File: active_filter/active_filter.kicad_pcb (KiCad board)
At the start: 2 copper layers, 26.4 x 22.9 mm, 15 parts, among them J0 Conn_01x03_MountingPin, J1 Conn_01x03_MountingPin, U1 ADA4062-2

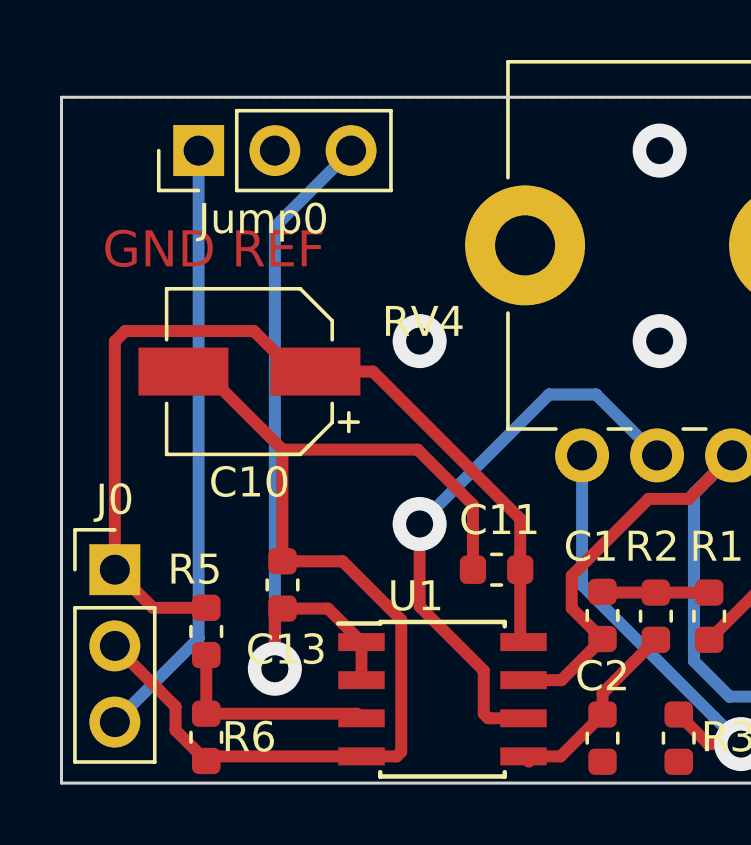
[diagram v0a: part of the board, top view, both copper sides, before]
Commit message: added second decoupling cap and swapped symbols
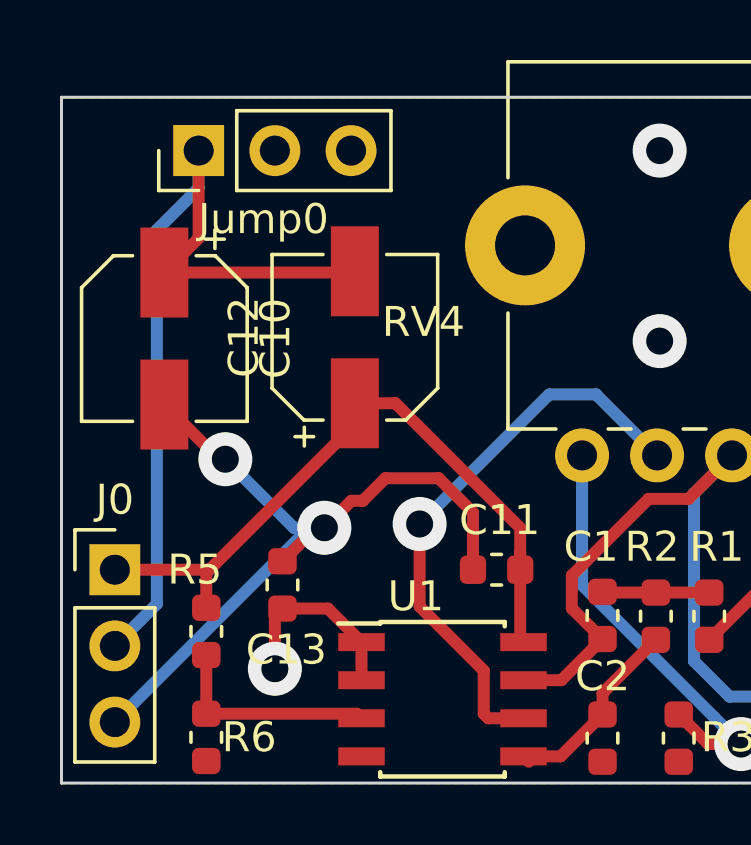
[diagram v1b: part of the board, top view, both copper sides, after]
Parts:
- added C12: 10u, default-footprints:CP_Elec_5x5.4, F.Cu at (30.9, 37.7)
- J0: value Conn_01x03_MountingPin -> Conn_01x03
- moved C10 3.04 mm to (24.5, 37.8), turned to 270 degrees
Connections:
- C10 pad 1: VCC -> GND
- J0 pad 2: VEE -> GND
- J0 pad 3: GND -> VEE
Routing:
- net REF: track 24.8 -> 6.48 mm
- net VEE: track 38.3 -> 26.6 mm, vias 0 -> 2
- net GND: track 20.2 -> 29.3 mm
- net VCC: track 31.6 -> 23.1 mm
- net COM: vias 3 -> 2
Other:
- board text removed: "GND REF"

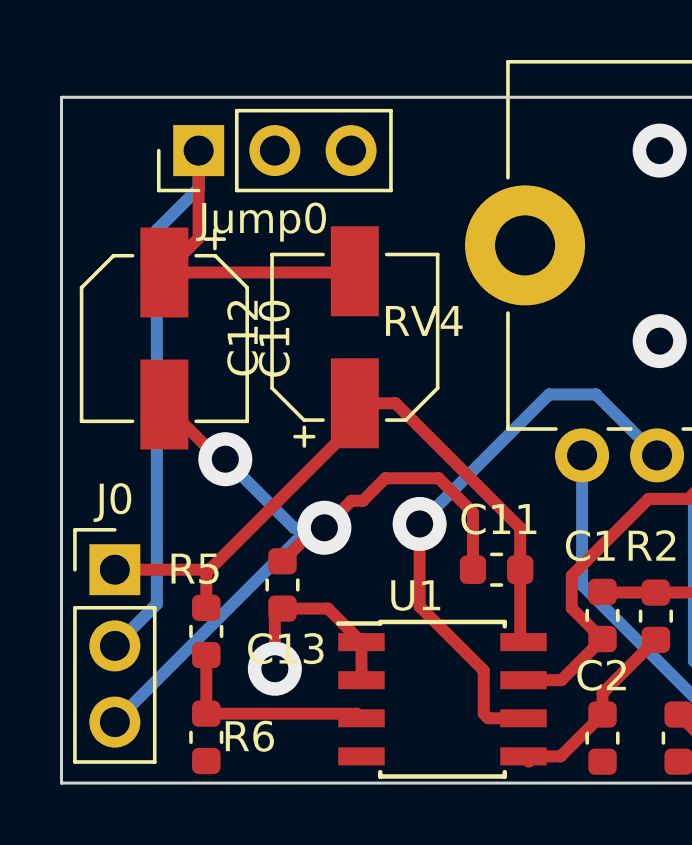
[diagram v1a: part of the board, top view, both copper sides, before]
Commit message: added missing traces
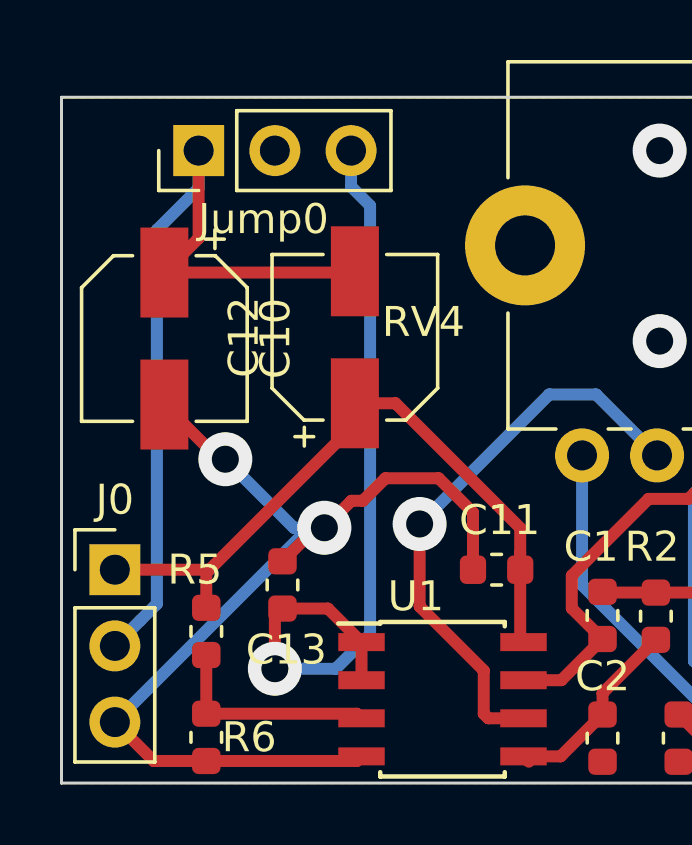
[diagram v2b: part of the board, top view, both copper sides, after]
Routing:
- net REF: track 6.48 -> 26.5 mm
- net VEE: track 26.6 -> 35.4 mm
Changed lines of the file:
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@@
     (thickness 1.6)
     (drawings 4)
-    (tracks 86)
+    (tracks 95)
     (zones 0)
     (modules 16)
@@
     (aux_axis_origin 0 0)
     (grid_origin 21.082 52.578)
-    (visible_elements FFFFF77F)
+    (visible_elements FFFFFF7F)
     (pcbplotparams
       (layerselection 0x010fc_ffffffff)
@@
   (segment (start 28.194 47.0155) (end 28.448 46.7615) (width 0.4) (layer F.Cu) (net 1))
   (segment (start 28.194 48.768) (end 28.194 47.0155) (width 0.4) (layer F.Cu) (net 1))
+  (segment (start 28.194 48.768) (end 30.226 48.768) (width 0.4) (layer B.Cu) (net 1))
+  (segment (start 30.226 48.768) (end 31.369 47.625) (width 0.4) (layer B.Cu) (net 1))
+  (segment (start 31.369 33.333081) (end 30.734 32.698081) (width 0.4) (layer B.Cu) (net 1))
+  (segment (start 30.734 32.698081) (end 30.734 31.496) (width 0.4) (layer B.Cu) (net 1))
+  (segment (start 31.369 47.625) (end 31.369 33.333081) (width 0.4) (layer B.Cu) (net 1))
   (segment (start 25.908 48.311) (end 25.908 50.2665) (width 0.4) (layer F.Cu) (net 2))
   (segment (start 30.9295 50.2665) (end 31.082 50.419) (width 0.4) (layer F.Cu) (net 2))
@@
   (segment (start 26.334 41.783) (end 24.511 39.96) (width 0.4) (layer F.Cu) (net 3))
   (segment (start 26.543 41.783) (end 26.334 41.783) (width 0.4) (layer F.Cu) (net 3))
+  (segment (start 30.9295 51.8415) (end 31.082 51.689) (width 0.4) (layer F.Cu) (net 3))
+  (segment (start 25.908 51.8415) (end 30.9295 51.8415) (width 0.4) (layer F.Cu) (net 3))
+  (segment (start 24.1555 51.8415) (end 22.86 50.546) (width 0.4) (layer F.Cu) (net 3))
+  (segment (start 25.908 51.8415) (end 24.1555 51.8415) (width 0.4) (layer F.Cu) (net 3))
   (segment (start 30.861 39.919) (end 32.216675 39.919) (width 0.4) (layer F.Cu) (net 7))
   (segment (start 36.373 44.891) (end 36.373 45.466) (width 0.4) (layer F.Cu) (net 7))

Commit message: Passermarken und Gerber hinzugefügt
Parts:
- added REF**: Fiducial_classic_Small_CopperBottom_Type2, Fiducial:Fiducial_classic_Small_CopperBottom_Type2, F.Cu at (18.9, 55.1)
- added REF**: Fiducial_classic_Small_CopperBottom_Type2, Fiducial:Fiducial_classic_Small_CopperBottom_Type2, F.Cu at (49.9, 55.0)
- added REF**: Fiducial_classic_Small_CopperBottom_Type2, Fiducial:Fiducial_classic_Small_CopperBottom_Type2, F.Cu at (49.9, 27.2)
- added REF**: Fiducial_classic_Small_CopperBottom_Type2, Fiducial:Fiducial_classic_Small_CopperBottom_Type2, F.Cu at (18.5, 27.4)
- added REF**: Fiducial_classic_Small_CopperTop_Type2, Fiducial:Fiducial_classic_Small_CopperTop_Type2, F.Cu at (18.5, 27.4)
- added REF**: Fiducial_classic_Small_CopperTop_Type2, Fiducial:Fiducial_classic_Small_CopperTop_Type2, F.Cu at (49.9, 27.2)
- added REF**: Fiducial_classic_Small_CopperTop_Type2, Fiducial:Fiducial_classic_Small_CopperTop_Type2, F.Cu at (49.9, 55.0)
- added REF**: Fiducial_classic_Small_CopperTop_Type2, Fiducial:Fiducial_classic_Small_CopperTop_Type2, F.Cu at (18.9, 55.1)
